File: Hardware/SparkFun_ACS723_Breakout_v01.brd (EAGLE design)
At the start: 24.1 x 15.2 mm, 19 parts, among them J1 455-1750-1-ND, U1 ACS723

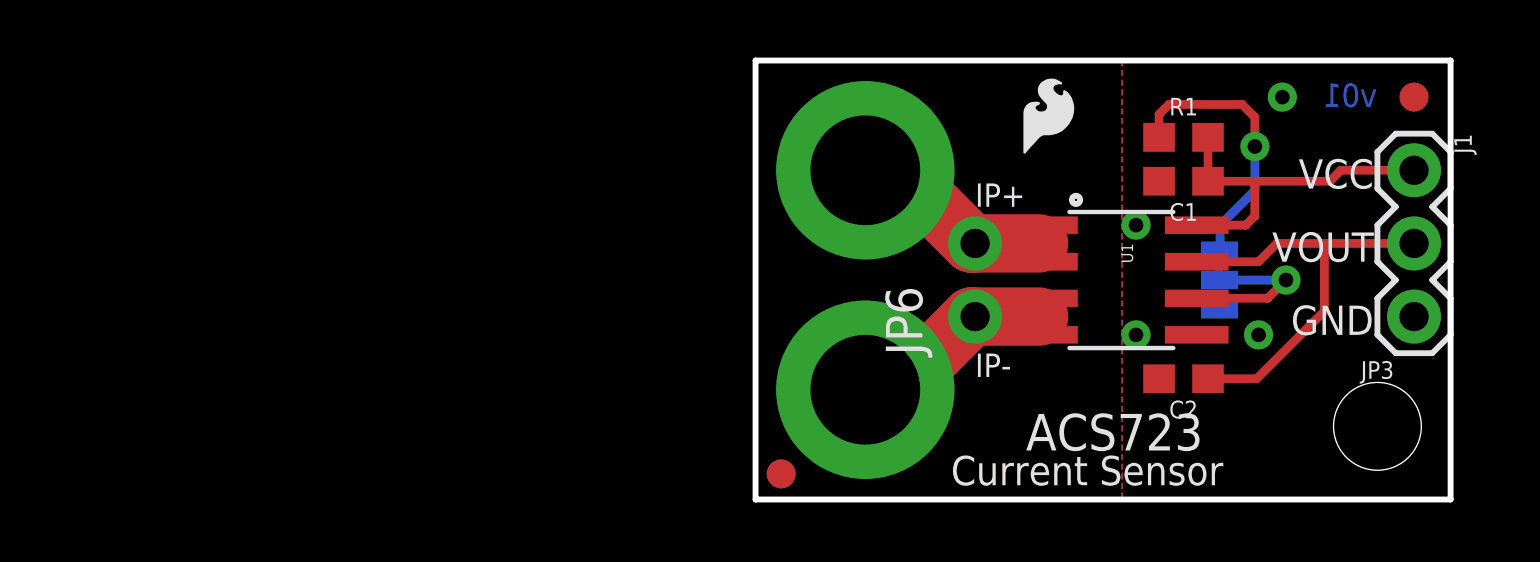
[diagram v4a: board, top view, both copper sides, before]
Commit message: v01 to v10 finalization
-added notes for bandwidth select
-added full IC name
-added small info partition in sch
-changed version numbers from v01 to v10
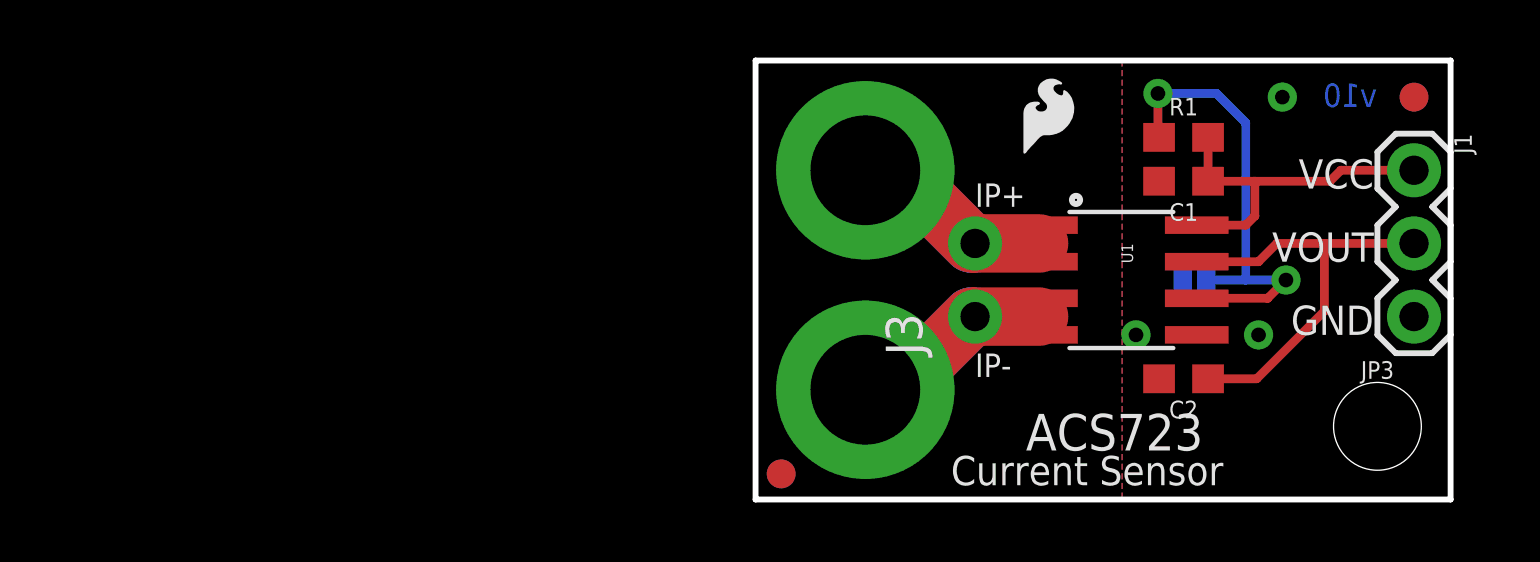
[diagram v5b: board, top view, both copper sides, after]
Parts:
- removed JP4: JUMPER-SMT_3_1-NC_TRACE_SILK, SparkFun-Jumpers:SMT-JUMPER_3_1-NC_TRACE_SILK
- added J2: (no value), SparkFun-Connectors:SMTSO-256-ET
- JP1: value (none) -> JUMPER-SMT_2_NO_SILK; device SparkFun-Connectors:SMTSO-256-ET -> SparkFun-Jumpers:SMT-JUMPER_2_NO_SILK
- moved JP1 12.0 mm to (15.2, 7.62), flipped to the bottom, turned to 180 degrees
- renumbered JP2 to J4, JP6 to J3
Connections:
- removed net N$3: JP4.3, R1.1
- net BW_SEL: now also JP1.2, R1.1; no longer JP4.2
- net GND: now also JP1.1; no longer JP4.1
- net IP+: now also J2.P$1; no longer JP1.P$1
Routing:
- net BW_SEL: track 5.67 -> 16.6 mm, vias 1 -> 2
- net N$3: track 9.60 -> 0.00 mm, vias 1 -> 0
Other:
- board text added: "v10"
- board text removed: "v01"
